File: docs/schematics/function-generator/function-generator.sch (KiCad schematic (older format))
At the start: 4 parts

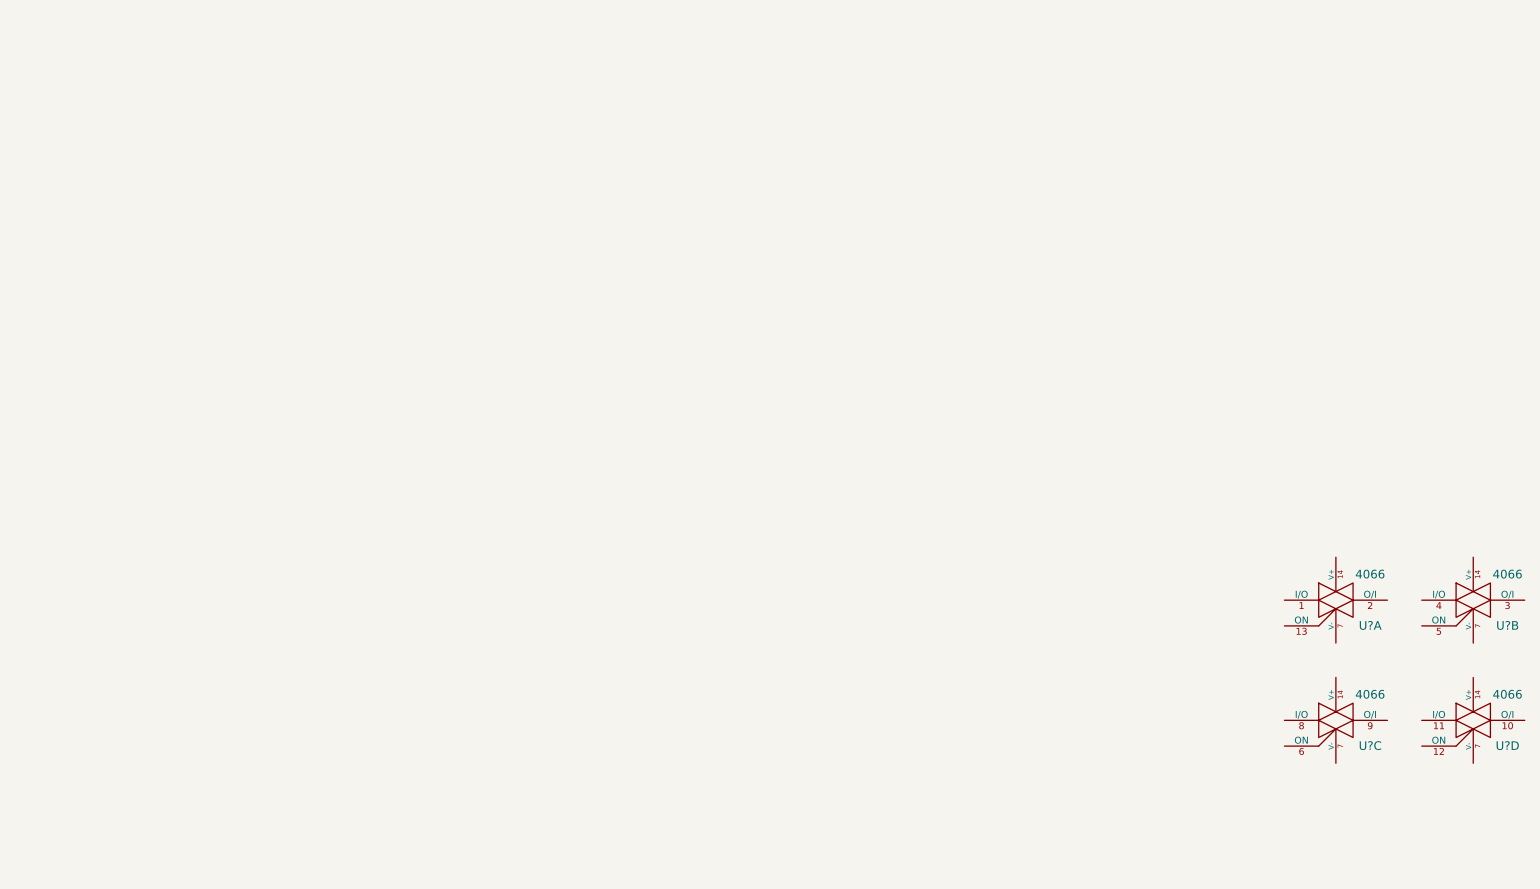
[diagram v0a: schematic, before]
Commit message: schematics, datasheets, and documentation
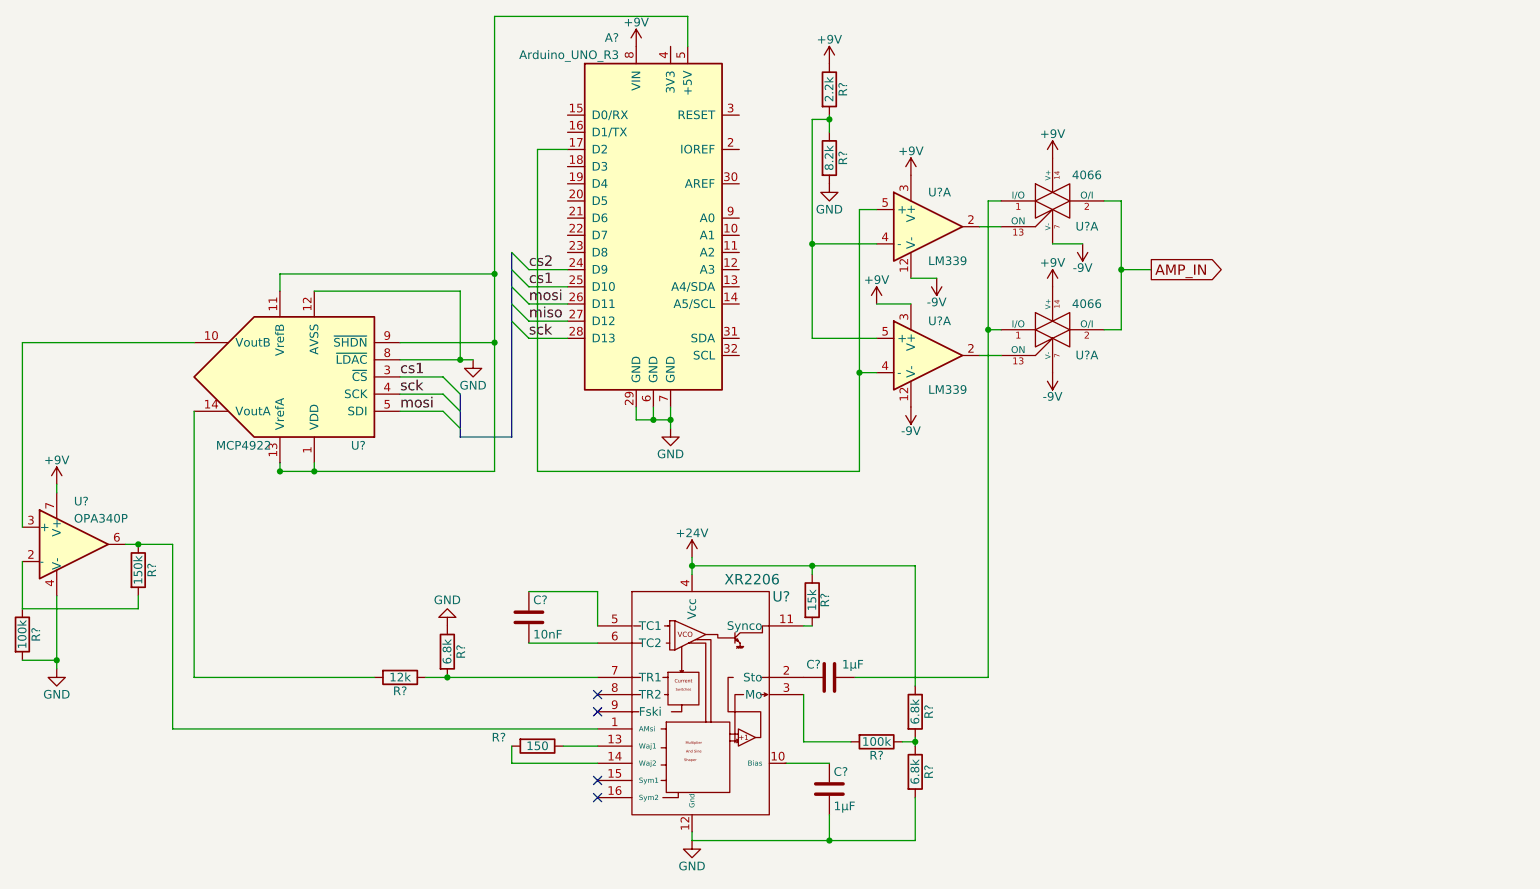
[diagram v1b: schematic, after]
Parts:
- removed U? (x4): 4066, symbol 4066
- added A?: Arduino_UNO_R3, Modules:Arduino_UNO_R3, symbol Arduino_UNO_R3
- added C? (x2): 1µF, symbol C
- added C?: 10nF, symbol C
- added R?: 15k, symbol R
- added R?: 150, symbol R
- added R? (x3): 6.8k, symbol R
- added R?: 12k, symbol R
- added R? (x2): 100k, symbol R
- added R?: 150k, symbol R
- added R?: 8.2k, symbol R
- added R?: 2.2k, symbol R
- added U?: XR2206, symbol XR2206
- added U?: MCP4922, symbol MCP4922
- added U? (x2): 4066, symbol 4066
- added U? (x2): LM339, symbol LM339
- added U?: OPA340P, Housings_DIP:DIP-8_W7.62mm, symbol OPA340P
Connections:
- new net: R?.1, U?.1 (AMsi), U?.6
- new net: C?.1, U?.10 (Bias)
- new net: R?.2, U?.11 (Synco)
- new net: R?.1, U?.13 (Waj1)
- new net: R?.2, U?.14 (Waj2)
- new net: C?.1, U?.2 (Sto)
- new net: R?.2, U?.3 (Mo)
- new net: C?.1, U?.5 (TC1)
- new net: C?.2, U?.6 (TC2)
- new net: R?.1, R?.2, U?.7 (TR1)
- new net: A?.5 (+5V), U?.1 (VDD), U?.11 (VrefB), U?.13 (VrefA), U?.9 (~SHDN~)
- new net: U?.10 (VoutB), U?.3 (+)
- new net: R?.2, U?.14 (VoutA)
- new net: C?.2, U?.1 (I/O), U?.1 (I/O)
- new net: U?.13 (ON), U?.2 (x2)
- new net: R?.1, R?.2, U?.4 (-), U?.5 (+)
- new net: A?.17 (D2), U?.4 (-), U?.5 (+)
- new net: R?.1, R?.1, R?.2
- new net: R?.1, R?.2, U?.2 (-)
- new net +24V: R?.1, R?.1, U?.4 (Vcc)
- new net +9V: A?.8 (VIN), R?.1, U?.14 (V+), U?.14 (V+), U?.3 (V+), U?.3 (V+), U?.7 (V+)
- new net -9V: U?.12 (V-), U?.12 (V-), U?.7 (V-), U?.7 (V-)
- new net AMP_IN: U?.2 (O/I), U?.2 (O/I)
- new net GND: A?.29 (GND), A?.6 (GND), A?.7 (GND), C?.2, R?.1, R?.2, R?.2, R?.2, U?.12 (AVSS), U?.12 (Gnd), U?.4 (V-), U?.8 (~LDAC~)
- new net cs1: A?.25 (D10), U?.3 (~CS~)
- new net cs2: A?.24 (D9)
- new net miso: A?.27 (D12)
- new net mosi: A?.26 (D11), U?.5 (SDI)
- new net sck: A?.28 (D13), U?.4 (SCK)
- no-connect marks 0 -> 4
